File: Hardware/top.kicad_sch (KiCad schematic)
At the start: 0 parts

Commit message: Schematic Done
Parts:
- added R10, R11: 100k, Resistor_SMD:R_0402_1005Metric, symbol Device:R
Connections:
- net ESP32-S31/I2C1-SCL: now also R10.2
- net ESP32-S31/I2C1-SDA: now also R11.2
- new net +3.3V: R10.1, R11.1
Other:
- added sheet DC-DC (power.kicad_sch)
- sheet ESP32-S31 ports: added BACKLIGHTen; removed none
- sheet USB and Cells ports: added I2C-SCL, I2C-SDA; removed none
- company: (none) -> Motion Composites
- title: (none) -> Strain Gauge Data Logger

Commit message: Layout cleaned
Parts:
- renumbered R11 to R1, R10 to R3
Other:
- sheet ESP32-S31 ports: added USB_D+, USB_D-; removed USB-Dn, USB-Dp
- sheet USB and Cells ports: added USB_D+, USB_D-; removed USB-Dn, USB-Dp
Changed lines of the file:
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@@
 		(in_pos_files yes)
 		(dnp no)
-		(property "Reference" "R11"
+		(property "Reference" "R1"
 			(at 135.636 62.484 90)
 			(show_name no)
@@
 			(project "esp32-V2"
 				(path "/cee18f8d-8618-44b5-96f4-3f3967d85a92"
-					(reference "R11")
+					(reference "R1")
 					(unit 1)
 				)
@@
 		(in_pos_files yes)
 		(dnp no)
-		(property "Reference" "R10"
+		(property "Reference" "R3"
 			(at 128.778 62.484 90)
 			(show_name no)
@@
 			(project "esp32-V2"
 				(path "/cee18f8d-8618-44b5-96f4-3f3967d85a92"
-					(reference "R10")
+					(reference "R3")
 					(unit 1)
 				)
@@
 			)
 		)
-		(pin "USB-Dn" bidirectional
-			(at 109.22 110.49 0)
-			(effects
-				(font
-					(size 1.524 1.524)
-				)
-				(justify right)
-			)
-		)
-		(pin "USB-Dp" bidirectional
-			(at 109.22 107.95 0)
-			(effects
-				(font
-					(size 1.524 1.524)
-				)
-				(justify right)
-			)
-		)
 		(pin "I2C-SCL" input
 			(at 109.22 116.84 0)
@@
 		(pin "I2C-SDA" bidirectional
 			(at 109.22 119.38 0)
+			(effects
+				(font
+					(size 1.524 1.524)
+				)
+				(justify right)
+			)
+		)
+		(pin "USB_D+" bidirectional
+			(at 109.22 107.95 0)
+			(effects
+				(font
+					(size 1.524 1.524)
+				)
+				(justify right)
+			)
+		)
+		(pin "USB_D-" bidirectional
+			(at 109.22 110.49 0)
 			(effects
 				(font
@@
 			)
 		)
-		(pin "USB-Dn" bidirectional
+		(pin "USB_D-" bidirectional
 			(at 158.75 110.49 180)
 			(effects
@@
 			)
 		)
-		(pin "USB-Dp" bidirectional
+		(pin "USB_D+" bidirectional
 			(at 158.75 107.95 180)
 			(effects

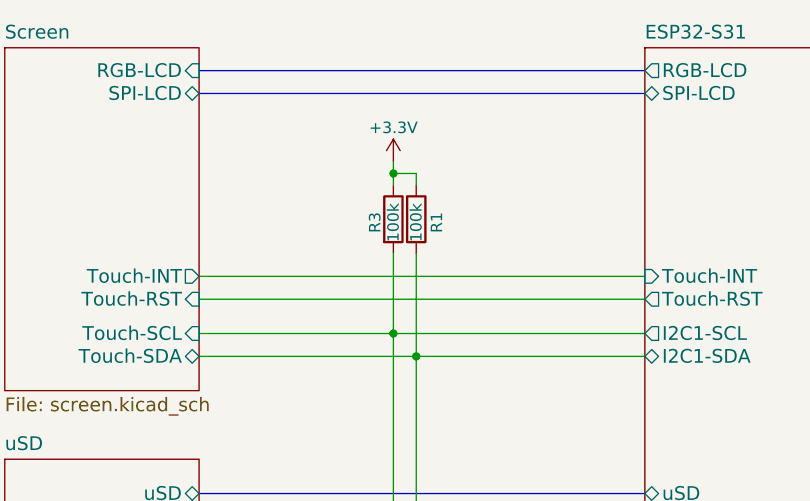
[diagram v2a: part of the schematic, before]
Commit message: Update de la librairy et du BOM
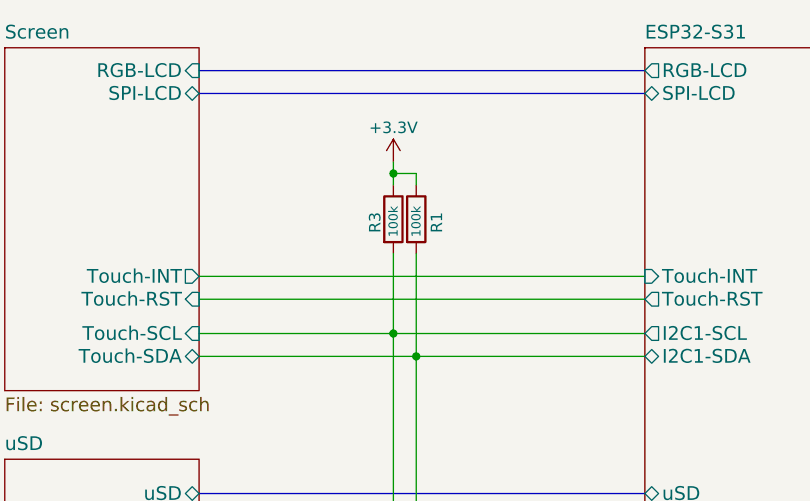
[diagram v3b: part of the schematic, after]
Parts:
- R1, R3: symbol Device:R -> YV-library:RES100KM-00; KiLib_Generator SMD_2terminal_chip_molded -> (none); PartNumber (none) -> 0402WGF1003TCE
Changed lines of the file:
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@@
 	)
 	(symbol
-		(lib_id "Device:R")
+		(lib_id "YV-library:RES100KM-00")
 		(at 133.35 60.96 0)
 		(unit 1)
@@
 		)
 		(property "Value" "100k"
-			(at 133.35 63.5 90)
+			(at 133.35 61.214 90)
 			(show_name no)
 			(do_not_autoplace no)
 			(effects
 				(font
-					(size 1.27 1.27)
+					(size 1.016 1.016)
 				)
-				(justify left)
 			)
 		)
@@
 			)
 		)
-		(property "Description" "Resistor"
+		(property "Description" "Res, 100kΩ, 50V, 62.5mW, Thick Film, ±1%, ±100ppm/℃, 0402,  -55℃~+155℃"
 			(at 133.35 60.96 0)
 			(hide yes)
@@
 			(effects
 				(font
-					(size 1.27 1.27)
+					(size 1.016 1.016)
 				)
 			)
 		)
-		(property "KiLib_Generator" "SMD_2terminal_chip_molded"
-			(at 133.35 60.96 0)
+		(property "LCSC" "C25741"
+			(at 131.572 60.96 90)
 			(hide yes)
 			(show_name no)
@@
 			)
 		)
-		(property "LCSC" "C25741"
+		(property "PartNumber" "0402WGF1003TCE"
 			(at 133.35 60.96 0)
 			(hide yes)
@@
 			(effects
 				(font
-					(size 1.524 1.524)
+					(size 1.27 1.27)
 				)
 			)
@@
 	)
 	(symbol
-		(lib_id "Device:R")
+		(lib_id "YV-library:RES100KM-00")
 		(at 130.81 60.96 0)
 		(unit 1)
@@
 		)
 		(property "Value" "100k"
-			(at 130.81 63.5 90)
+			(at 130.81 61.214 90)
 			(show_name no)
 			(do_not_autoplace no)
 			(effects
 				(font
-					(size 1.27 1.27)
+					(size 1.016 1.016)
 				)
-				(justify left)
 			)
 		)
@@
 			)
 		)
-		(property "Description" "Resistor"
+		(property "Description" "Res, 100kΩ, 50V, 62.5mW, Thick Film, ±1%, ±100ppm/℃, 0402,  -55℃~+155℃"
+			(at 130.81 60.96 0)
+			(hide yes)
+			(show_name no)
+			(do_not_autoplace no)
+			(effects
+				(font
+					(size 1.016 1.016)
+				)
+			)
+		)
+		(property "LCSC" "C25741"
+			(at 129.032 60.96 90)
+			(hide yes)
+			(show_name no)
+			(do_not_autoplace no)
+			(effects
+				(font
+					(size 1.524 1.524)
+				)
+			)
+		)
+		(property "PartNumber" "0402WGF1003TCE"
 			(at 130.81 60.96 0)
 			(hide yes)
@@
 				)
 			)
-		)
-		(property "KiLib_Generator" "SMD_2terminal_chip_molded"
-			(at 130.81 60.96 0)
-			(hide yes)
-			(show_name no)
-			(do_not_autoplace no)
-			(effects
-				(font
-					(size 1.524 1.524)
-				)
-			)
-		)
-		(property "LCSC" "C25741"
-			(at 130.81 60.96 0)
-			(hide yes)
-			(show_name no)
-			(do_not_autoplace no)
-			(effects
-				(font
-					(size 1.524 1.524)
-				)
-			)
